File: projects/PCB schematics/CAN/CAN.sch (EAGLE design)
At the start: 0 parts

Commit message: CAN - Initial draft.
Vertical connectors chosen. Several options should be compliant with this PCB footprint.
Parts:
- added BAMOCAR_D3, BMS_1, BMS_2, CSCU, ECU, SCU: (no value), con-subd:F09VP
- added GND: 5566-2, con-molex:5566-2
- added J1, J2: (no value), con-lstb:MA03-1
- added R1, R2: (no value), rcl:R-US_R0805
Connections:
- new net CANH: BAMOCAR_D3.7, BMS_1.7, BMS_2.7, CSCU.7, ECU.7, J1.2, J2.2, SCU.7
- new net CANL: BAMOCAR_D3.2, BMS_1.2, BMS_2.2, CSCU.2, ECU.2, R1.2, R2.2, SCU.2
- new net GND: BAMOCAR_D3.3, BAMOCAR_D3.6, BMS_1.3, BMS_1.6, BMS_2.3, BMS_2.6, CSCU.3, CSCU.6, ECU.3, ECU.6, GND-1.S, GND-2.S, SCU.3, SCU.6
- new net N$2: J2.3
- new net N$3: J2.1, R2.1
- new net N$4: J1.1, R1.1
- new net N$6: J1.3

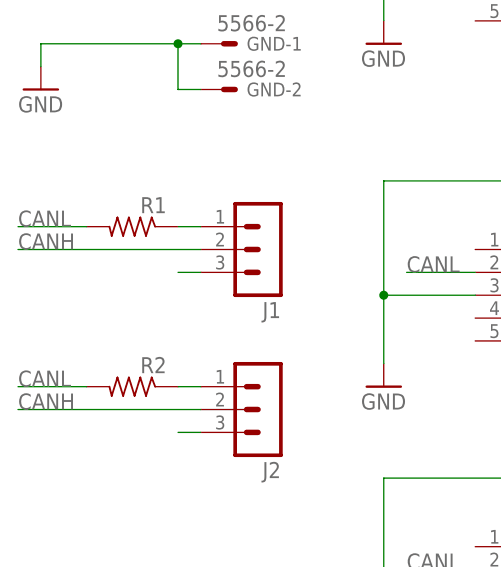
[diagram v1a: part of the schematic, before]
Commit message: CAN - Added in resistor values.
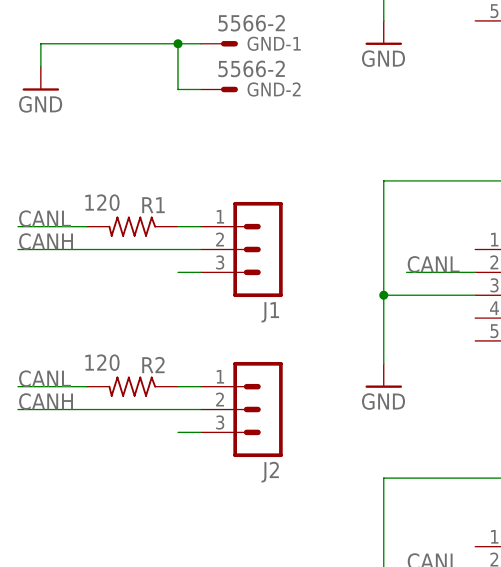
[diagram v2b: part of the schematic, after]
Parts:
- R1, R2: value (none) -> 120
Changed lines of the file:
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@@
 <part name="GND6" library="supply1" library_urn="urn:adsk.eagle:library:371" deviceset="GND" device=""/>
 <part name="GND7" library="supply1" library_urn="urn:adsk.eagle:library:371" deviceset="GND" device=""/>
-<part name="R1" library="rcl" library_urn="urn:adsk.eagle:library:334" deviceset="R-US_" device="R0805" package3d_urn="urn:adsk.eagle:package:23553/2"/>
-<part name="R2" library="rcl" library_urn="urn:adsk.eagle:library:334" deviceset="R-US_" device="R0805" package3d_urn="urn:adsk.eagle:package:23553/2"/>
+<part name="R1" library="rcl" library_urn="urn:adsk.eagle:library:334" deviceset="R-US_" device="R0805" package3d_urn="urn:adsk.eagle:package:23553/2" value="120"/>
+<part name="R2" library="rcl" library_urn="urn:adsk.eagle:library:334" deviceset="R-US_" device="R0805" package3d_urn="urn:adsk.eagle:package:23553/2" value="120"/>
 </parts>
 <sheets>
@@
 <instance part="R1" gate="G$1" x="20.32" y="50.8" smashed="yes" rot="MR0">
 <attribute name="NAME" x="24.13" y="52.2986" size="1.778" layer="95" rot="MR0"/>
-<attribute name="VALUE" x="24.13" y="47.498" size="1.778" layer="96" rot="MR0"/>
+<attribute name="VALUE" x="19.05" y="52.578" size="1.778" layer="96" rot="MR0"/>
 </instance>
 <instance part="R2" gate="G$1" x="20.32" y="33.02" smashed="yes" rot="MR0">
 <attribute name="NAME" x="24.13" y="34.5186" size="1.778" layer="95" rot="MR0"/>
-<attribute name="VALUE" x="24.13" y="29.718" size="1.778" layer="96" rot="MR0"/>
+<attribute name="VALUE" x="19.05" y="34.798" size="1.778" layer="96" rot="MR0"/>
 </instance>
 </instances>

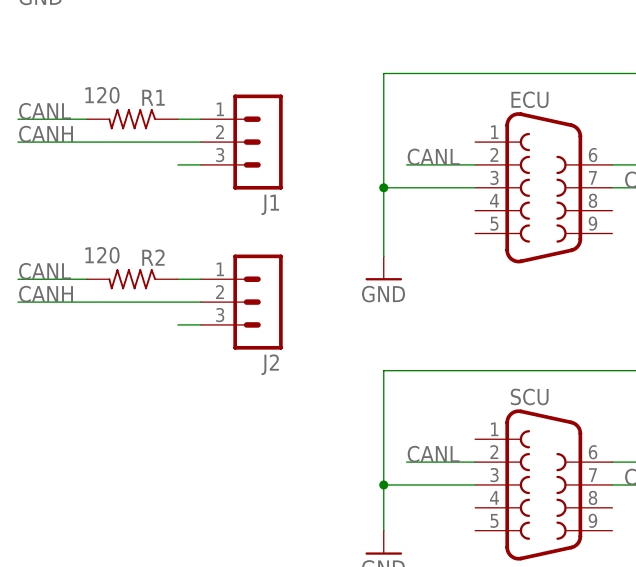
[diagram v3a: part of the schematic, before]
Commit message: PROJ - Silkscreen modifications - 50%.
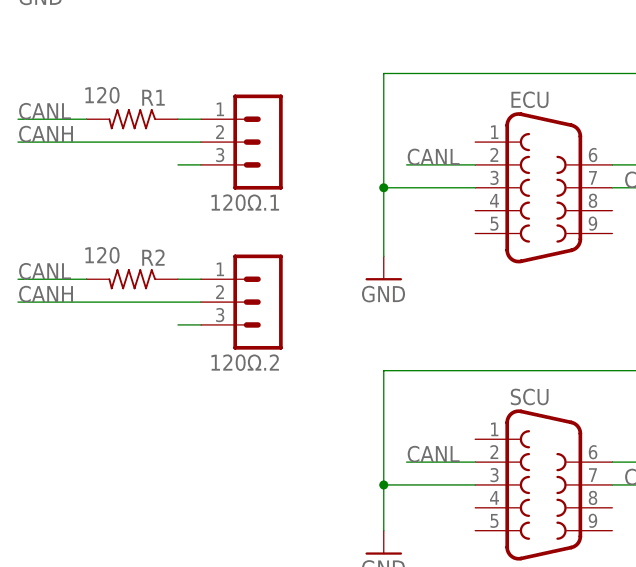
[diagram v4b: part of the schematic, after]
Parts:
- renumbered J1 to 120Ω.1, J2 to 120Ω.2
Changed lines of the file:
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@@
 <part name="GND" library="con-molex" library_urn="urn:adsk.eagle:library:165" deviceset="5566-2" device="" package3d_urn="urn:adsk.eagle:package:8078583/1"/>
 <part name="GND3" library="supply1" library_urn="urn:adsk.eagle:library:371" deviceset="GND" device=""/>
-<part name="J1" library="con-lstb" library_urn="urn:adsk.eagle:library:162" deviceset="MA03-1" device="" package3d_urn="urn:adsk.eagle:package:8339/1"/>
-<part name="J2" library="con-lstb" library_urn="urn:adsk.eagle:library:162" deviceset="MA03-1" device="" package3d_urn="urn:adsk.eagle:package:8339/1"/>
+<part name="120Ω.1" library="con-lstb" library_urn="urn:adsk.eagle:library:162" deviceset="MA03-1" device="" package3d_urn="urn:adsk.eagle:package:8339/1"/>
+<part name="120Ω.2" library="con-lstb" library_urn="urn:adsk.eagle:library:162" deviceset="MA03-1" device="" package3d_urn="urn:adsk.eagle:package:8339/1"/>
 <part name="GND4" library="supply1" library_urn="urn:adsk.eagle:library:371" deviceset="GND" device=""/>
 <part name="GND5" library="supply1" library_urn="urn:adsk.eagle:library:371" deviceset="GND" device=""/>
@@
 <attribute name="VALUE" x="7.62" y="63.5" size="1.778" layer="96"/>
 </instance>
-<instance part="J1" gate="G$1" x="35.56" y="48.26" smashed="yes" rot="R180">
+<instance part="120Ω.1" gate="G$1" x="35.56" y="48.26" smashed="yes" rot="R180">
 <attribute name="VALUE" x="36.83" y="55.88" size="1.778" layer="96" rot="R180"/>
 <attribute name="NAME" x="36.83" y="42.418" size="1.778" layer="95" rot="R180"/>
 </instance>
-<instance part="J2" gate="G$1" x="35.56" y="30.48" smashed="yes" rot="R180">
+<instance part="120Ω.2" gate="G$1" x="35.56" y="30.48" smashed="yes" rot="R180">
 <attribute name="VALUE" x="36.83" y="38.1" size="1.778" layer="96" rot="R180"/>
 <attribute name="NAME" x="36.83" y="24.638" size="1.778" layer="95" rot="R180"/>
@@
 <net name="N$2" class="0">
 <segment>
-<pinref part="J2" gate="G$1" pin="3"/>
+<pinref part="120Ω.2" gate="G$1" pin="3"/>
 <wire x1="27.94" y1="27.94" x2="25.4" y2="27.94" width="0.1524" layer="91"/>
 </segment>
@@
 <segment>
 <pinref part="R2" gate="G$1" pin="1"/>
-<pinref part="J2" gate="G$1" pin="1"/>
+<pinref part="120Ω.2" gate="G$1" pin="1"/>
 <wire x1="25.4" y1="33.02" x2="27.94" y2="33.02" width="0.1524" layer="91"/>
 </segment>
@@
 <segment>
 <pinref part="R1" gate="G$1" pin="1"/>
-<pinref part="J1" gate="G$1" pin="1"/>
+<pinref part="120Ω.1" gate="G$1" pin="1"/>
 <wire x1="25.4" y1="50.8" x2="27.94" y2="50.8" width="0.1524" layer="91"/>
 </segment>
@@
 <net name="N$6" class="0">
 <segment>
-<pinref part="J1" gate="G$1" pin="3"/>
+<pinref part="120Ω.1" gate="G$1" pin="3"/>
 <wire x1="25.4" y1="45.72" x2="27.94" y2="45.72" width="0.1524" layer="91"/>
 </segment>
@@
 <net name="CANH" class="0">
 <segment>
-<pinref part="J2" gate="G$1" pin="2"/>
+<pinref part="120Ω.2" gate="G$1" pin="2"/>
 <wire x1="27.94" y1="30.48" x2="7.62" y2="30.48" width="0.1524" layer="91"/>
 <label x="7.62" y="30.48" size="1.778" layer="95"/>
 </segment>
 <segment>
-<pinref part="J1" gate="G$1" pin="2"/>
+<pinref part="120Ω.1" gate="G$1" pin="2"/>
 <wire x1="7.62" y1="48.26" x2="27.94" y2="48.26" width="0.1524" layer="91"/>
 <label x="7.62" y="48.26" size="1.778" layer="95"/>
